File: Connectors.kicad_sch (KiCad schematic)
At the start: 5 parts, among them J1 MR60PW, J2 MR60PW, J3 XT60PW-F, J5 XT60PW-M

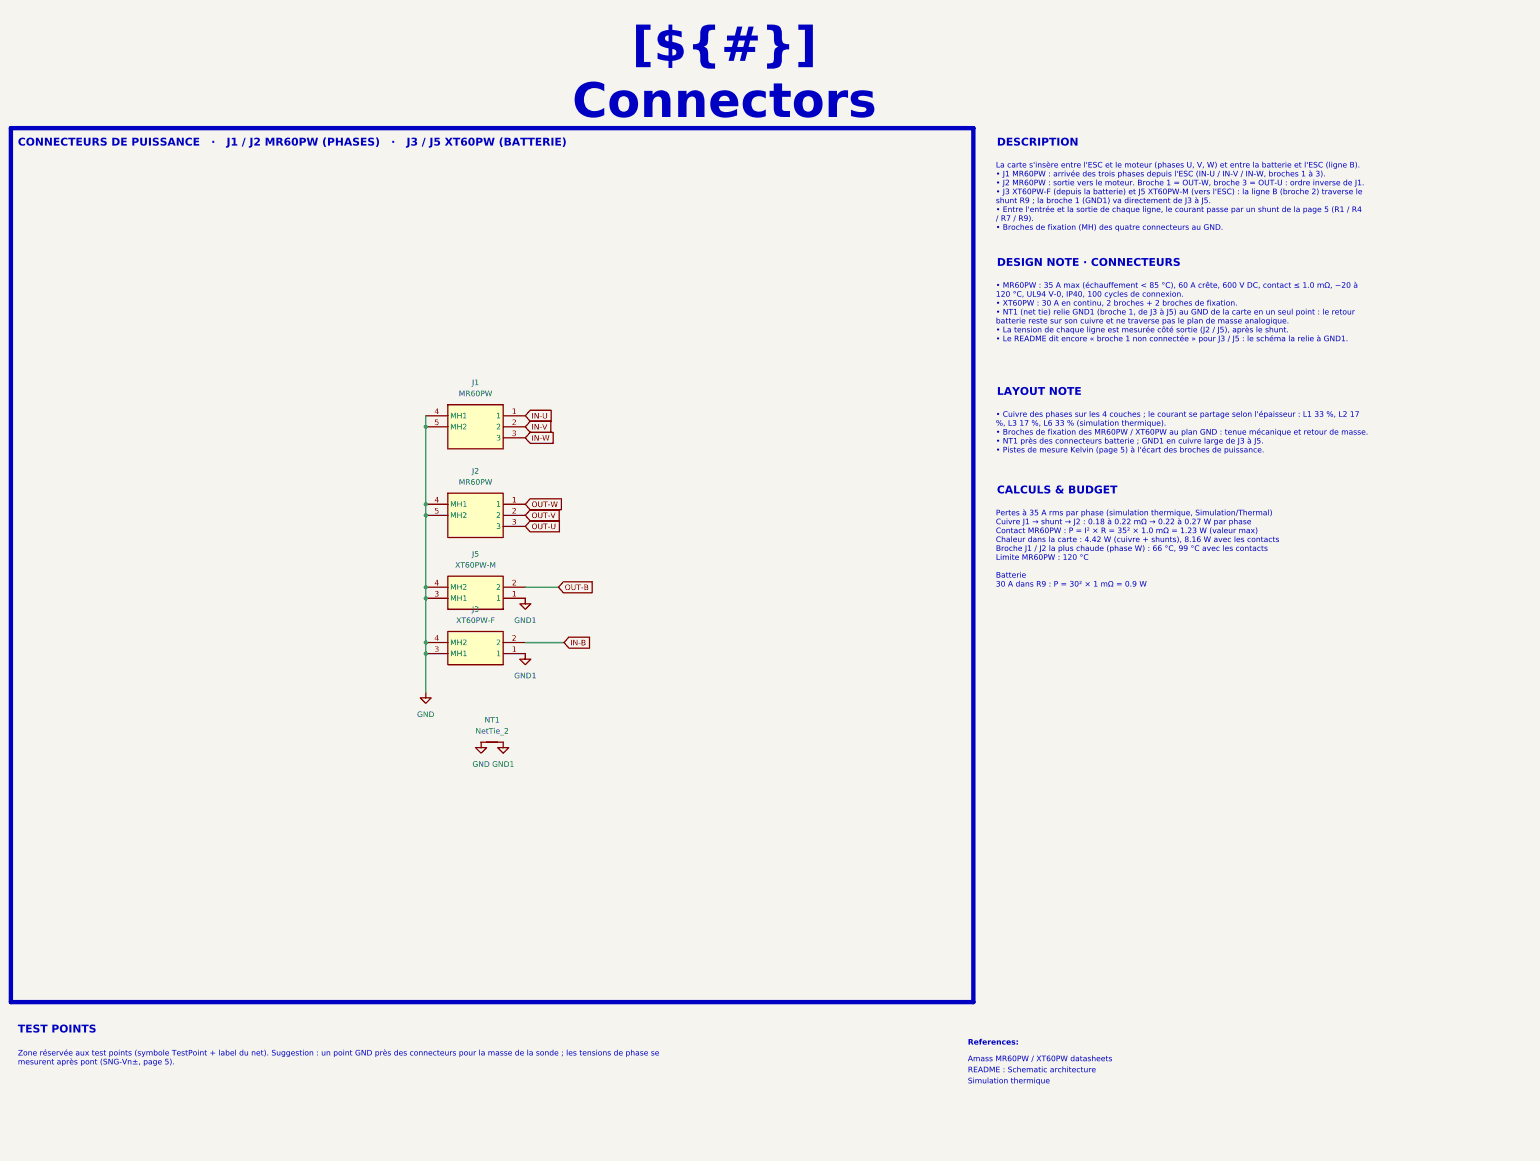
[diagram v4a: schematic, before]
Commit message: Wire the AD7606C-18 digital side to host header J4, add test points
- AD7606C-18: software mode (OS0-2 high), serial (PAR/SER SEL high),
  REF SELECT low; CONVST, BUSY, RESET, CS, SCLK, SDI, FRSTDATA and
  DOUTA-D to J4 (2x8 pin header 2.54 mm, horizontal), +3.3V on J4 pin 1
- AD7606C-18 AGND pin 26 and REFGND pin 46 on GND
- Test points TP1-TP16: rails, INA241 outputs, CONVST, BUSY
- Nets renamed SHUNT_*, INA_*, ADC_*; net colours in the project
- LT3045-1 footprint: thermal vias numbered as exposed pad 13
- PCB updated from the schematic; ADC_* digital nets not routed yet
- README template / CHANGELOG: status, J4 pinout, design review 1 and 2
  fixed, new finding 9 (VDRIVE above AVCC + 0.3 V at power-up),
  4 channels / 8 ADC inputs

Co-Authored-By: Claude Opus 5.5 <noreply@anthropic.com>
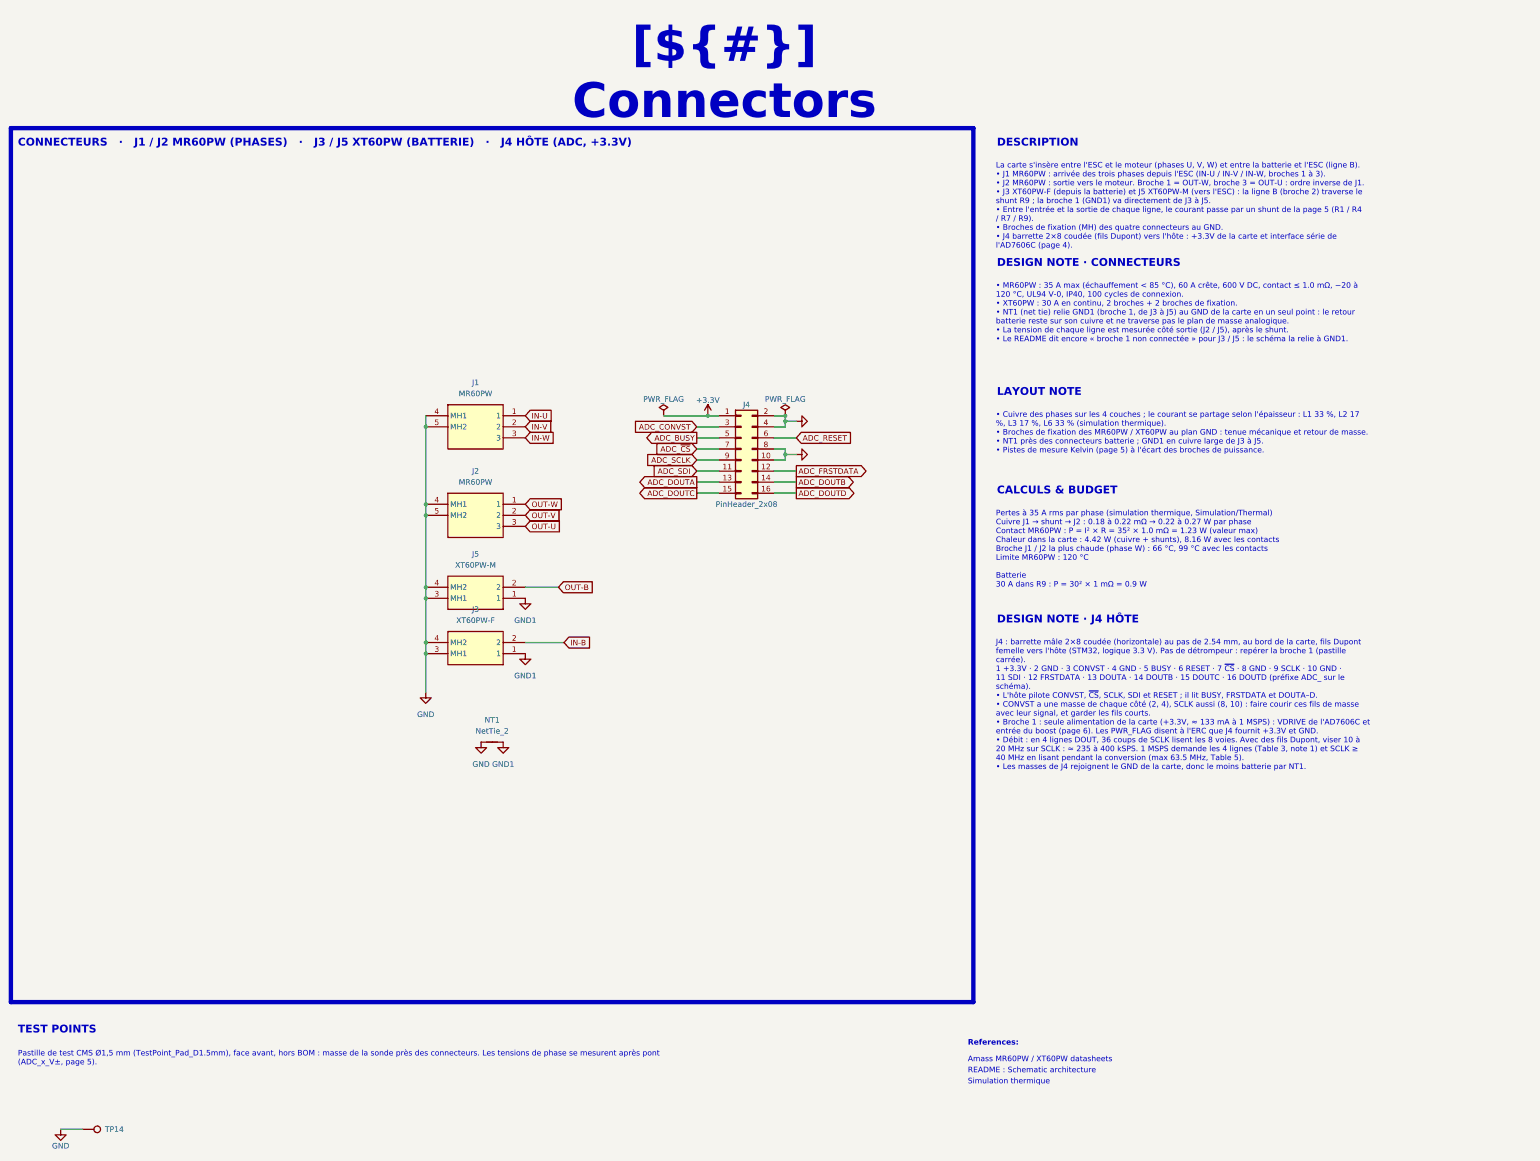
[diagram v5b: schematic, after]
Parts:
- added J4: PinHeader_2x08, OPEN_PHASE:PinHeader_2x08_P2.54mm_Horizontal, symbol OPEN_PHASE:Conn_02x08_Odd_Even
- added TP14: TestPoint, OPEN_PHASE:TestPoint_Pad_D1.5mm, symbol OPEN_PHASE:TestPoint
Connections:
- net GND: now also J4.10 (Pin_10), J4.2 (Pin_2), J4.4 (Pin_4), J4.8 (Pin_8), TP14.1
- new net +3.3V: J4.1 (Pin_1)
- new net ADC_BUSY: J4.5 (Pin_5)
- new net ADC_CONVST: J4.3 (Pin_3)
- new net ADC_DOUTA: J4.13 (Pin_13)
- new net ADC_DOUTB: J4.14 (Pin_14)
- new net ADC_DOUTC: J4.15 (Pin_15)
- new net ADC_DOUTD: J4.16 (Pin_16)
- new net ADC_FRSTDATA: J4.12 (Pin_12)
- new net ADC_RESET: J4.6 (Pin_6)
- new net ADC_SCLK: J4.9 (Pin_9)
- new net ADC_SDI: J4.11 (Pin_11)
- new net ADC_~{CS}: J4.7 (Pin_7)

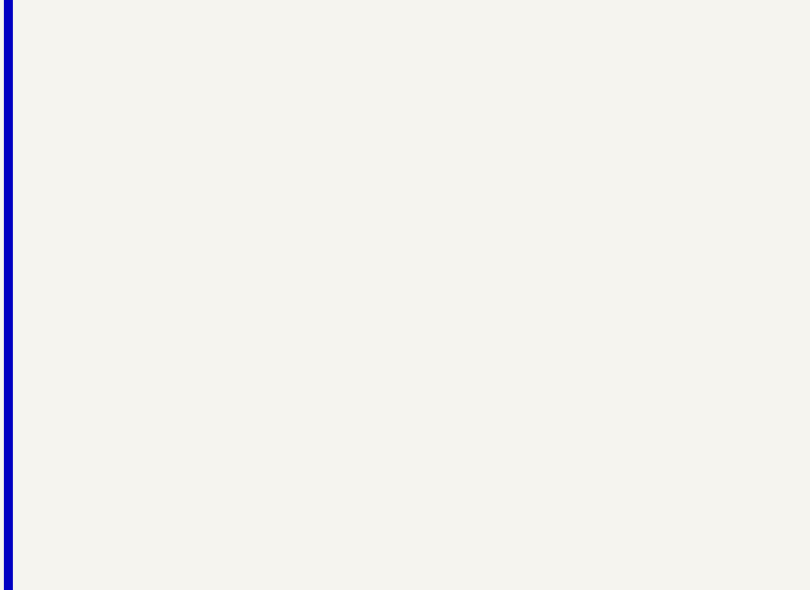
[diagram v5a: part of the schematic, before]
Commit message: Add rail indicator LEDs, test point tags and OSHW logo
- Schematic: D1, D3-D5 rail indicator LEDs on +2.5VA, +5VA, +3.3V and
  +6V. Series resistors R35 750 R, R37 1.5k, R36 3.3k, R38 4.3k: about
  1 mA each with a Wurth 150060RS75000 (red, 1.78 V at 1 mA).
- PCB F.SilkS: rail name beside each LED (Airborne 0.8 mm knockout).
- PCB B.SilkS: J4-style tags on the 10 placed test points (pill that
  wraps the pad, net name in Arial Black knockout), OSHW logo LOGO2
  (board only) next to the bottom logo.
- lib: OSHW-Logo_7.5x8mm_SilkScreen added to the project footprints.
- Images: 3D spin animation in the blue / white colours.

DRC and schematic parity counts are unchanged by the silkscreen work.

Co-Authored-By: Claude Opus 5.5 <noreply@anthropic.com>
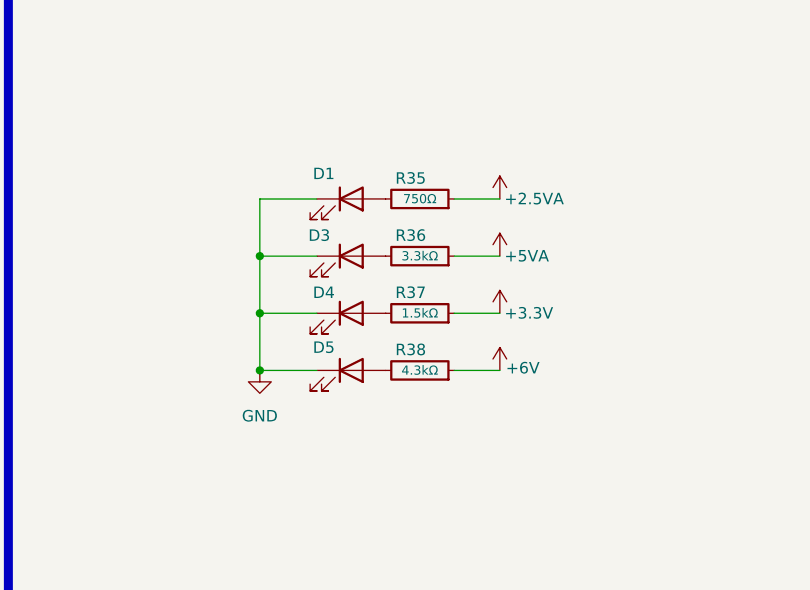
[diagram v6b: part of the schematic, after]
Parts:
- added D1, D3, D4, D5: LED, LED_SMD:LED_0603_1608Metric, symbol Device:LED
- added R35: 750Ω, OPEN_PHASE:R_0603_1608Metric, symbol OPEN_PHASE:R
- added R36: 3.3kΩ, OPEN_PHASE:R_0603_1608Metric, symbol OPEN_PHASE:R
- added R37: 1.5kΩ, OPEN_PHASE:R_0603_1608Metric, symbol OPEN_PHASE:R
- added R38: 4.3kΩ, OPEN_PHASE:R_0603_1608Metric, symbol OPEN_PHASE:R
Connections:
- net +3.3V: now also R37.2
- net GND: now also D1.1 (K), D3.1 (K), D4.1 (K), D5.1 (K)
- new net: D4.2 (A), R37.1
- new net: D5.2 (A), R38.1
- new net: D3.2 (A), R36.1
- new net: D1.2 (A), R35.1
- new net +2.5VA: R35.2
- new net +5VA: R36.2
- new net +6V: R38.2
